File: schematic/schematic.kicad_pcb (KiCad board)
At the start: 4 copper layers, 100 x 100 mm, 260 parts, among them J1 Conn_01x04, J10 Conn_01x03, J11 Conn_01x02, J12 Conn_01x02, J13 Conn_01x02, J14 Conn_01x02, J15 Conn_01x02, J16 Conn_01x02, J17 Conn_01x04, J18 Conn_02x13_Odd_Even, J2 Conn_01x04, J3 Conn_01x04, J4 Conn_01x04, J5 Conn_01x04, J6 Conn_01x06, J7 Conn_01x03, J8 Screw_Terminal_01x02, J9 Conn_01x03, Q1 PSMN1R7-30YL, Q2 PSMN1R7-30YL, Q3 NCV8402, Q4 NCV8402, SW1 SW_Push_Dual, SW2 SW_DIP_x03, U1 STM32F401VETx, U2 TMC2130, U3 TMC2130, U4 TMC2130, U5 TMC2130, U6 BD9E302EFJ, U7 BD9E302EFJ, U8 BD9E302EFJ, Y1 Crystal_GND24

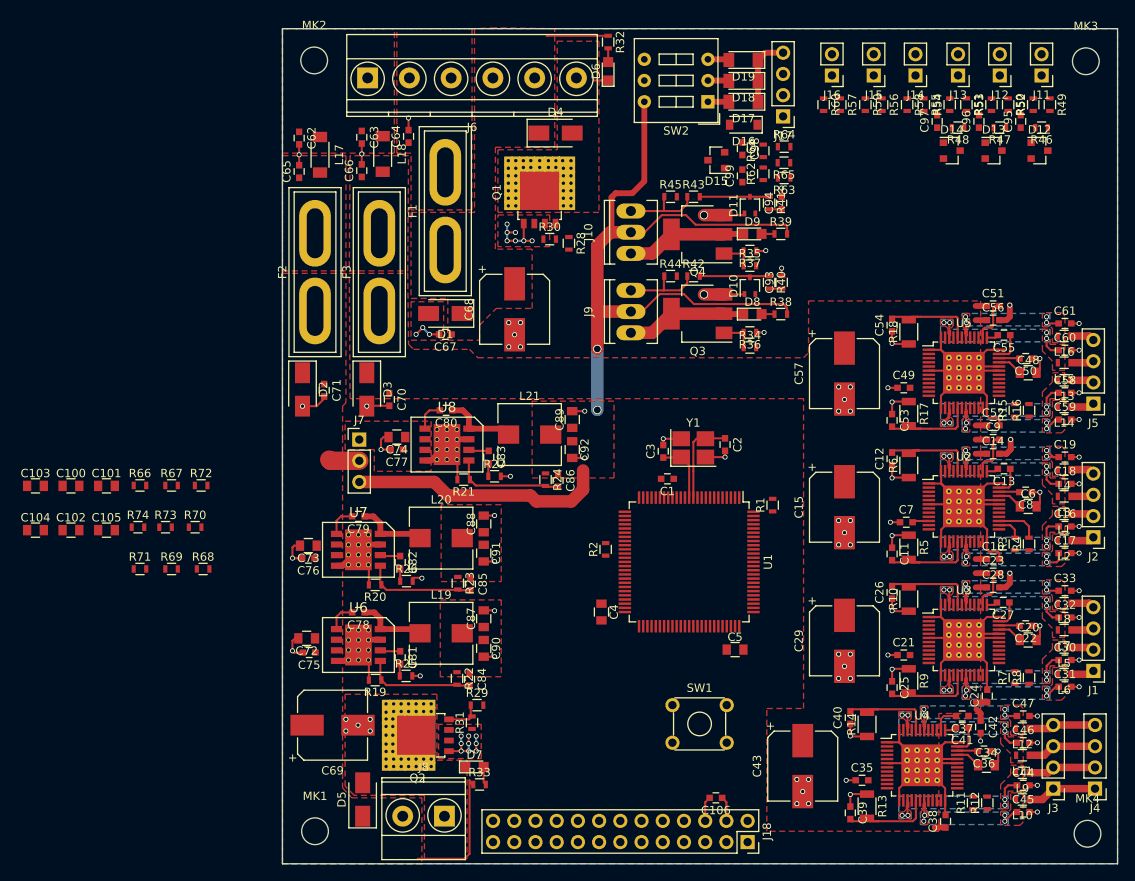
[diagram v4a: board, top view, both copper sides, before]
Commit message: main power plains routed
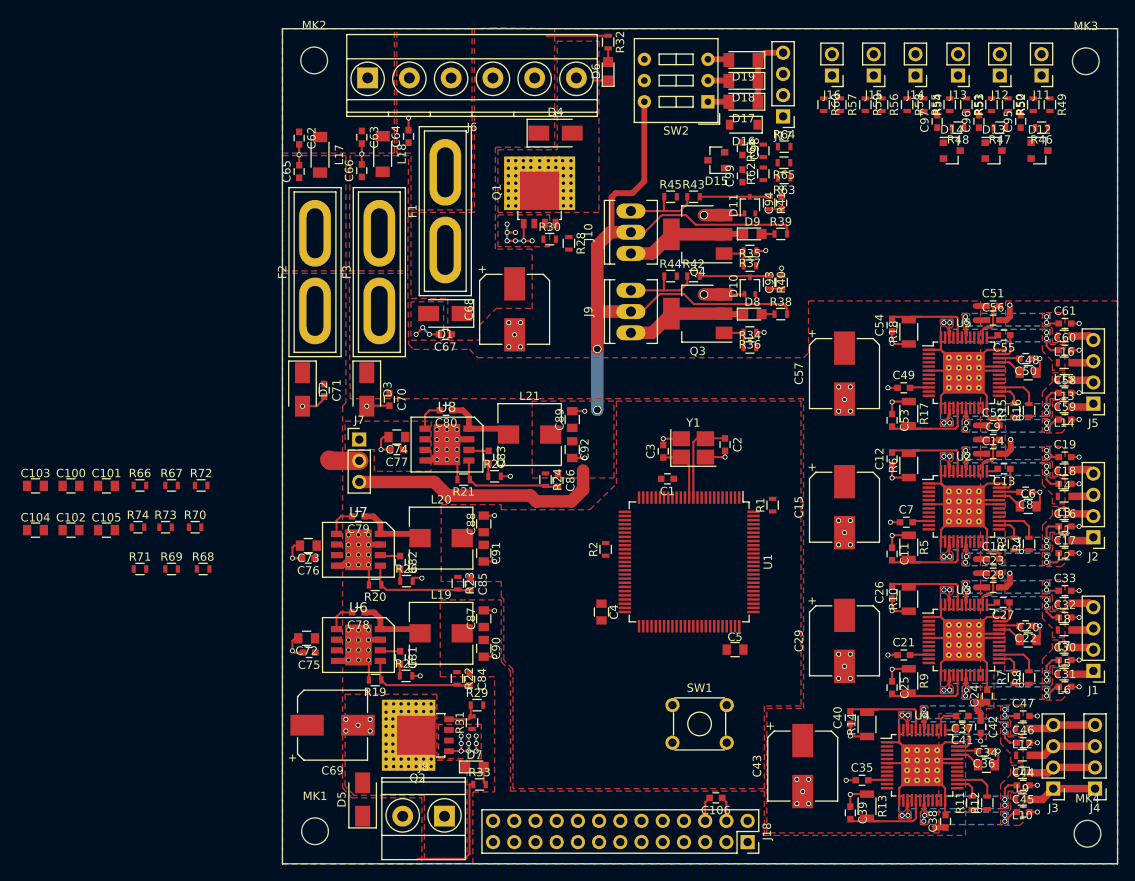
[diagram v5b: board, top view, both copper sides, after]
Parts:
- moved R11 0.10 mm to (247.6, 142.7)
- moved R15 0.10 mm to (252.6, 95.7)
- moved R3 0.10 mm to (252.6, 111.7)
- moved R7 0.10 mm to (252.6, 127.7)
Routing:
- net +3V3: track 2.01 -> 16.5 mm, vias 0 -> 4
- net YD1: track 0.00 -> 5.22 mm
- net ED1: track 0.00 -> 5.22 mm
- net ZD1: track 0.00 -> 5.22 mm
- net YD0: track 0.00 -> 3.04 mm
- net ZD0: track 0.00 -> 3.04 mm
- net ED0: track 0.00 -> 3.01 mm
- net VBUS: track 19.6 -> 18.9 mm
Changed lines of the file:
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@@
   (general
     (links 833)
-    (no_connects 209)
+    (no_connects 183)
     (area 133.3 48.325 267.04762 154.782382)
     (thickness 1.6)
     (drawings 4)
-    (tracks 961)
+    (tracks 1005)
     (zones 0)
     (modules 260)
@@
   )
   (module Resistors_SMD:R_0603 (layer F.Cu)
-    (at 252.7 111.7 90)
+    (at 252.6 111.7 90)
     (descr "Resistor SMD 0603, reflow soldering, Vishay (see dcrcw.pdf)")
     (tags "resistor 0603")
@@
   )
   (module Resistors_SMD:R_0603 (layer F.Cu)
-    (at 252.7 127.7 90)
+    (at 252.6 127.7 90)
     (descr "Resistor SMD 0603, reflow soldering, Vishay (see dcrcw.pdf)")
     (tags "resistor 0603")
@@
   )
   (module Resistors_SMD:R_0603 (layer F.Cu)
-    (at 247.7 142.7 90)
+    (at 247.6 142.7 90)
     (descr "Resistor SMD 0603, reflow soldering, Vishay (see dcrcw.pdf)")
     (tags "resistor 0603")
@@
   )
   (module Resistors_SMD:R_0603 (layer F.Cu)
-    (at 252.7 95.7 90)
+    (at 252.6 95.7 90)
     (descr "Resistor SMD 0603, reflow soldering, Vishay (see dcrcw.pdf)")
     (tags "resistor 0603")
@@
   (segment (start 250.8 105.95) (end 252.05 105.95) (width 0.25) (layer F.Cu) (net 7) (status 10))
   (segment (start 252.05 105.95) (end 253.3 107.2) (width 0.25) (layer F.Cu) (net 7))
+  (segment (start 249.4 143.45) (end 248.65 143.45) (width 0.25) (layer F.Cu) (net 8))
+  (segment (start 248.35 143.45) (end 248.5 143.6) (width 0.25) (layer F.Cu) (net 8))
+  (via (at 248.5 143.6) (size 0.6) (drill 0.4) (layers F.Cu B.Cu) (net 8))
+  (segment (start 248.35 143.45) (end 247.6 143.45) (width 0.25) (layer F.Cu) (net 8))
+  (segment (start 248.65 143.45) (end 248.5 143.6) (width 0.25) (layer F.Cu) (net 8))
+  (segment (start 254.4 128.45) (end 253.65 128.45) (width 0.25) (layer F.Cu) (net 8))
+  (segment (start 253.35 128.45) (end 253.5 128.6) (width 0.25) (layer F.Cu) (net 8))
+  (via (at 253.5 128.6) (size 0.6) (drill 0.4) (layers F.Cu B.Cu) (net 8))
+  (segment (start 253.35 128.45) (end 252.6 128.45) (width 0.25) (layer F.Cu) (net 8))
+  (segment (start 253.65 128.45) (end 253.5 128.6) (width 0.25) (layer F.Cu) (net 8))
+  (segment (start 254.4 112.45) (end 253.65 112.45) (width 0.25) (layer F.Cu) (net 8))
+  (segment (start 253.35 112.45) (end 253.5 112.6) (width 0.25) (layer F.Cu) (net 8))
+  (via (at 253.5 112.6) (size 0.6) (drill 0.4) (layers F.Cu B.Cu) (net 8))
+  (segment (start 253.35 112.45) (end 252.6 112.45) (width 0.25) (layer F.Cu) (net 8))
+  (segment (start 253.65 112.45) (end 253.5 112.6) (width 0.25) (layer F.Cu) (net 8))
+  (segment (start 252.6 96.45) (end 253.35 96.45) (width 0.25) (layer F.Cu) (net 8))
+  (segment (start 253.65 96.45) (end 253.5 96.6) (width 0.25) (layer F.Cu) (net 8))
+  (via (at 253.5 96.6) (size 0.6) (drill 0.4) (layers F.Cu B.Cu) (net 8))
+  (segment (start 253.65 96.45) (end 254.4 96.45) (width 0.25) (layer F.Cu) (net 8))
+  (segment (start 253.35 96.45) (end 253.5 96.6) (width 0.25) (layer F.Cu) (net 8))
+  (segment (start 237.4 139.95) (end 235.2 139.95) (width 0.25) (layer F.Cu) (net 8))
+  (segment (start 235.2 139.95) (end 235.15 140) (width 0.25) (layer F.Cu) (net 8))
+  (segment (start 242.4 92.95) (end 240.2 92.95) (width 0.25) (layer F.Cu) (net 8))
+  (segment (start 240.2 92.95) (end 240.15 93) (width 0.25) (layer F.Cu) (net 8))
+  (segment (start 242.4 124.95) (end 240.2 124.95) (width 0.25) (layer F.Cu) (net 8))
+  (segment (start 240.2 124.95) (end 240.15 125) (width 0.25) (layer F.Cu) (net 8))
   (segment (start 242.4 108.95) (end 240.6 108.95) (width 0.25) (layer F.Cu) (net 8) (status 10))
   (segment (start 240.6 108.95) (end 240.45 109.1) (width 0.25) (layer F.Cu) (net 8))
@@
   (segment (start 170.74 101.74) (end 170.6 101.6) (width 2.2) (layer F.Cu) (net 54))
   (segment (start 187.85 140.5) (end 187.7 140.5) (width 0.25) (layer F.Cu) (net 54) (status 30))
-  (segment (start 187.7 140.5) (end 187.4 140) (width 0.25) (layer F.Cu) (net 54) (status 10))
-  (segment (start 187.4 140) (end 187.4 148.8) (width 0.25) (layer F.Cu) (net 54))
+  (segment (start 187.7 140.5) (end 187.4 140.5) (width 0.25) (layer F.Cu) (net 54) (status 10))
+  (segment (start 187.4 140.5) (end 187.4 148.8) (width 0.25) (layer F.Cu) (net 54))
   (segment (start 187.4 148.8) (end 186.8 149.4) (width 0.25) (layer F.Cu) (net 54))
   (segment (start 186.8 149.4) (end 181.2 149.4) (width 0.25) (layer F.Cu) (net 54))
@@
   (segment (start 219.925 76.925) (end 217.875 76.925) (width 0.25) (layer F.Cu) (net 136))
   (segment (start 250.8 109.45) (end 252.15 109.45) (width 0.25) (layer F.Cu) (net 137) (status 10))
-  (segment (start 252.7 110) (end 252.7 110.95) (width 0.25) (layer F.Cu) (net 137))
-  (segment (start 252.15 109.45) (end 252.7 110) (width 0.25) (layer F.Cu) (net 137))
+  (segment (start 252.6 109.9) (end 252.6 110.95) (width 0.25) (layer F.Cu) (net 137) (status 20))
+  (segment (start 252.15 109.45) (end 252.6 109.9) (width 0.25) (layer F.Cu) (net 137))
   (segment (start 250.8 108.95) (end 253.75 108.95) (width 0.25) (layer F.Cu) (net 138) (status 10))
   (segment (start 254.4 109.6) (end 254.4 110.95) (width 0.25) (layer F.Cu) (net 138))
   (segment (start 253.75 108.95) (end 254.4 109.6) (width 0.25) (layer F.Cu) (net 138))
+  (segment (start 250.8 125.45) (end 252.15 125.45) (width 0.25) (layer F.Cu) (net 139))
+  (segment (start 252.6 125.9) (end 252.6 126.95) (width 0.25) (layer F.Cu) (net 139) (status 20))
+  (segment (start 252.15 125.45) (end 252.6 125.9) (width 0.25) (layer F.Cu) (net 139))
+  (segment (start 254.4 126.95) (end 254.4 125.6) (width 0.25) (layer F.Cu) (net 140))
+  (segment (start 253.75 124.95) (end 254.4 125.6) (width 0.25) (layer F.Cu) (net 140))
+  (segment (start 253.75 124.95) (end 250.8 124.95) (width 0.25) (layer F.Cu) (net 140))
+  (segment (start 245.8 140.45) (end 247.15 140.45) (width 0.25) (layer F.Cu) (net 141))
+  (segment (start 247.6 140.9) (end 247.6 141.95) (width 0.25) (layer F.Cu) (net 141) (status 20))
+  (segment (start 247.15 140.45) (end 247.6 140.9) (width 0.25) (layer F.Cu) (net 141))
+  (segment (start 245.8 139.95) (end 248.75 139.95) (width 0.25) (layer F.Cu) (net 142))
+  (segment (start 249.4 140.6) (end 249.4 141.95) (width 0.25) (layer F.Cu) (net 142))
+  (segment (start 248.75 139.95) (end 249.4 140.6) (width 0.25) (layer F.Cu) (net 142))
+  (segment (start 250.8 93.45) (end 252.15 93.45) (width 0.25) (layer F.Cu) (net 143))
+  (segment (start 252.6 94) (end 252.6 94.95) (width 0.25) (layer F.Cu) (net 143) (status 20))
+  (segment (start 252.15 93.45) (end 252.6 94) (width 0.25) (layer F.Cu) (net 143))
+  (segment (start 250.8 92.95) (end 253.75 92.95) (width 0.25) (layer F.Cu) (net 144))
+  (segment (start 254.4 93.6) (end 254.4 94.95) (width 0.25) (layer F.Cu) (net 144))
+  (segment (start 253.75 92.95) (end 254.4 93.6) (width 0.25) (layer F.Cu) (net 144))
   (segment (start 248.6 132.85) (end 248.6 132) (width 0.7) (layer F.Cu) (net 174))
   (segment (start 248.6 132) (end 248.1 131.5) (width 0.7) (layer F.Cu) (net 174))
@@
         (xy 180.1 87.8) (xy 180.7 88.4) (xy 187.4 88.4) (xy 188.4 89.4) (xy 227.4 89.4)
         (xy 228 88.8) (xy 228 82.6) (xy 248.6 82.6) (xy 248.6 132) (xy 243.6 132)
-        (xy 243.6 146.1) (xy 223 146.1) (xy 223 131.4) (xy 227.4 131.4) (xy 227.4 94.3)
+        (xy 243.6 146.3) (xy 223 146.3) (xy 223 131.4) (xy 227.4 131.4) (xy 227.4 94.3)
         (xy 173.1 94.3) (xy 173 79.3) (xy 180 79.3)
       )
@@
     (polygon
       (pts
-        (xy 183.9 118.4) (xy 191.2 118.4) (xy 191.2 127.6) (xy 183.9 127.6)
+        (xy 265 150) (xy 187.8 150) (xy 187.8 141.4) (xy 190.4 141.4) (xy 190.4 127.6)
+        (xy 183.9 127.6) (xy 183.9 118.4) (xy 191.2 118.4) (xy 191.2 125.8) (xy 192.3 126.9)
+        (xy 192.3 141.3) (xy 222.7 141.3) (xy 222.7 146.6) (xy 246.8 146.6) (xy 246.8 135.1)
+        (xy 249.3 135.1) (xy 249.3 131.4) (xy 250.2 131.4) (xy 250.2 126.9) (xy 251.5 126.9)
+        (xy 251.6 82.6) (xy 265 82.6)
       )
     )
@@
     (polygon
       (pts
-        (xy 184 116.2) (xy 191.2 116.2) (xy 191.2 107) (xy 184 107)
+        (xy 227.1 131.1) (xy 222.7 131.1) (xy 222.7 141) (xy 192.6 141) (xy 192.6 126.7)
+        (xy 191.5 125.6) (xy 191.5 118.3) (xy 191.2 118) (xy 191.2 116.2) (xy 184 116.2)
+        (xy 184 107) (xy 191.2 107) (xy 191.2 107.6) (xy 201.8 107.6) (xy 205 104.5)
+        (xy 205 94.6) (xy 227.1 94.6)
       )
     )

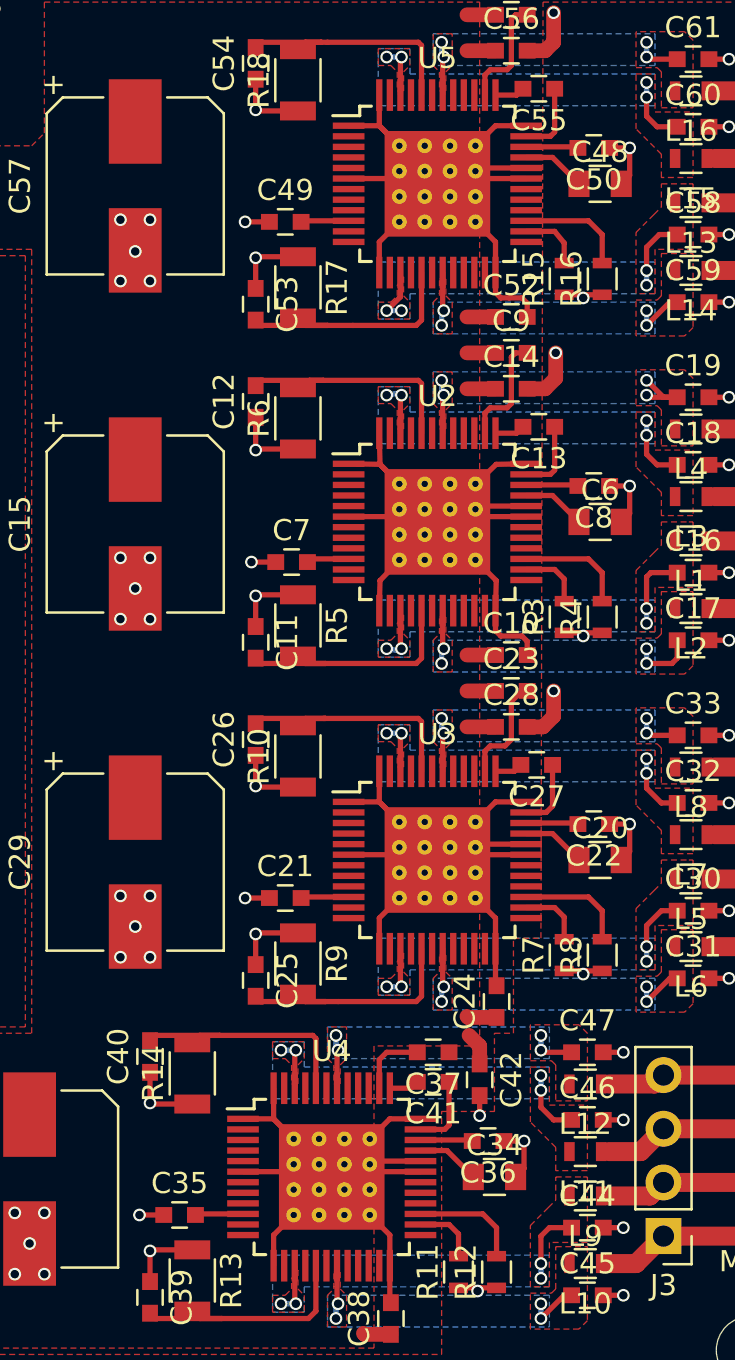
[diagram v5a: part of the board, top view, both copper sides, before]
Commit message: Started initial spi routing
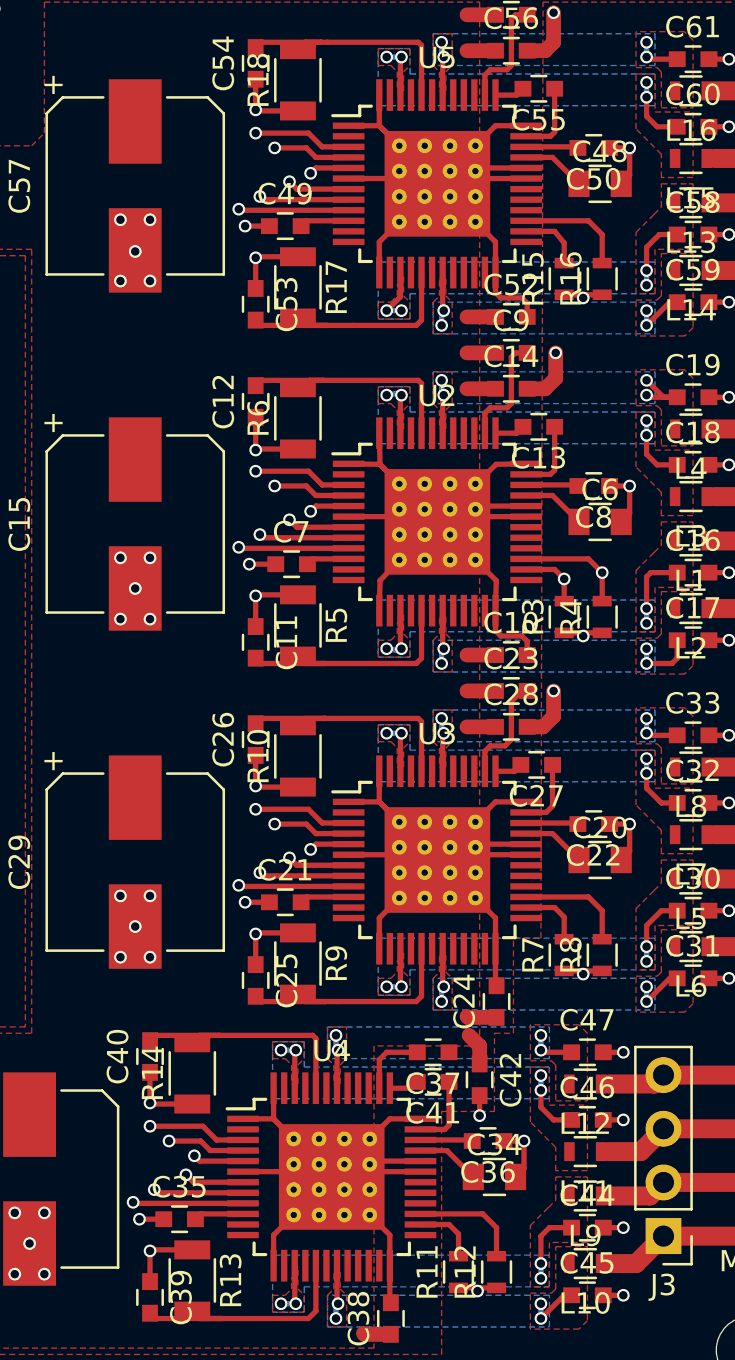
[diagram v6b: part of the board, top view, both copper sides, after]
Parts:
- moved C21 0.20 mm to (239.4, 125.2)
- moved C49 0.20 mm to (239.4, 93.2)
- moved C35 0.20 mm to (234.4, 140.2)
- moved C7 0.10 mm to (239.7, 109.2)
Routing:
- net SCK: track 0.00 -> 46.7 mm, vias 0 -> 4
- net MOSI: track 0.00 -> 43.7 mm, vias 0 -> 4
- net MISO: track 0.00 -> 40.1 mm, vias 0 -> 4
- net YDIR: track 0.00 -> 5.22 mm, vias 0 -> 1
- net XDIR: track 0.00 -> 5.22 mm, vias 0 -> 1
- net EDIR: track 0.00 -> 5.22 mm, vias 0 -> 1
- net ZDIR: track 0.00 -> 5.22 mm, vias 0 -> 1
- net YSS: track 0.00 -> 4.67 mm, vias 0 -> 1
- net XSS: track 0.00 -> 4.67 mm, vias 0 -> 1
- net ESS: track 0.00 -> 4.67 mm, vias 0 -> 1
- net ZSS: track 0.00 -> 4.67 mm, vias 0 -> 1
- net YSTEP: track 0.00 -> 4.26 mm, vias 0 -> 1
- net XSTEP: track 0.00 -> 4.26 mm, vias 0 -> 1
- net ESTEP: track 0.00 -> 4.26 mm, vias 0 -> 1
- net ZSTEP: track 0.00 -> 4.26 mm, vias 0 -> 1
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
